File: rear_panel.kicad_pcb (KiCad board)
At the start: 2 copper layers, 165.5 x 30.6 mm, 5 parts

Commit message: Front and rear layout done
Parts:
- moved REF** 0.46 mm to (69.4, 105.8)
- moved REF** 0.46 mm to (225.0, 105.8)
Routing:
- net GND: vias 140 -> 142
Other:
- outline, holes or cut-outs redrawn
- board text added: "10"
- board text added: "14"
- board text added: "15"
- board text added: "4"
- board text added: "9"
- board text removed: "1k"
- board text removed: "GPIO10"
- board text removed: "GPIO14"
- board text removed: "GPIO15"
- board text removed: "GPIO4"
- board text removed: "GPIO9"

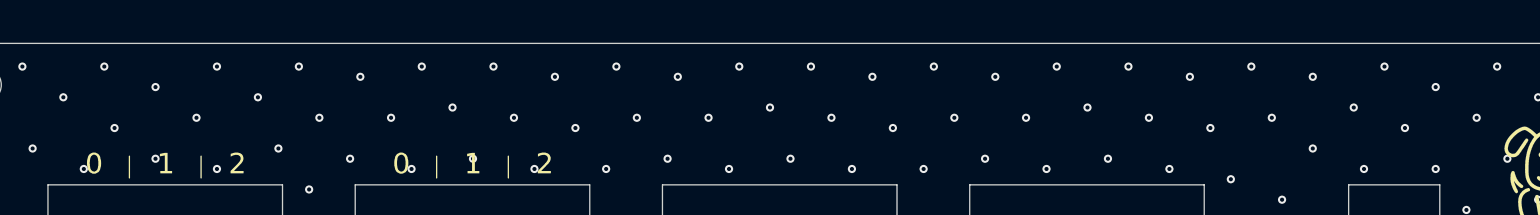
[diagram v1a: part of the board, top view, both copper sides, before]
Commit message: Added KiBuzzard labels
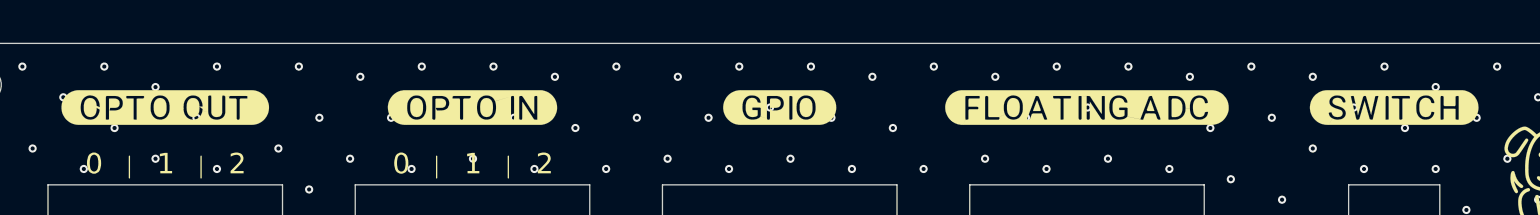
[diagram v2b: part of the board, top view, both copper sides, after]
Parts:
- added ?: , buzzardLabel, F.Cu at (177.2, 108.0)
- added ?: , buzzardLabel, F.Cu at (147.2, 108.0)
- added ?: , buzzardLabel, F.Cu at (87.2, 108.0)
- added ?: , buzzardLabel, F.Cu at (207.2, 108.0)
- added ?: , buzzardLabel, F.Cu at (117.2, 108.0)
